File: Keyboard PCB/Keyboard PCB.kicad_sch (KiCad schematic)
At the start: 9 parts, among them SW1 SW_Push, SW2 SW_Push, SW3 SW_Push, SW4 SW_Push, SW5 SW_Push, SW6 SW_Push, U1 MOUDLE-SEEEDUINO-XIAO

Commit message: Who needs autosaves?
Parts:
- removed D1, D2: SK6812MINI-E, footprints:SK6812MINI-E_fixed, symbol SK6812MINI-E:SK6812MINI-E
- added D1, D2: SK6812MINI, LED_SMD:LED_SK6812MINI_PLCC4_3.5x3.5mm_P1.75mm, symbol LED:SK6812MINI
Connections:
- net +5V: now also D1.4 (VDD), D2.4 (VDD)
- net GND: now also D1.2 (VSS), D2.2 (VSS)
- net at U1.5 (PA8_A4_D4_SDA): now also D1.3 (DIN)
- new net: D1.1 (DOUT), D2.3 (DIN)

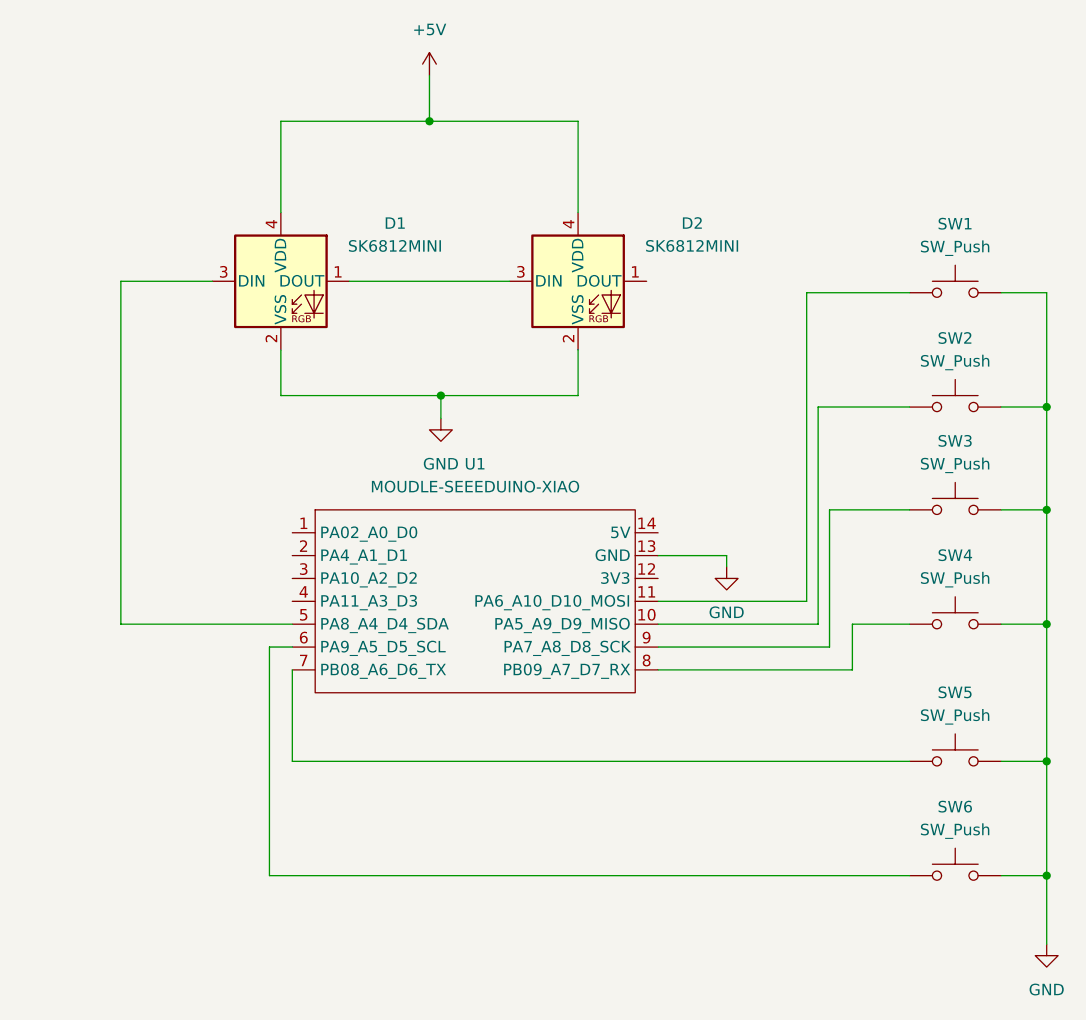
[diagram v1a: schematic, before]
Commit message: Adjusted wiring
I flipped the XIAO microcontroller because I was worried it would mess up the build process if it was on the bottom. For some reason the tutorial says to put it on the back side but most people just put it on top.
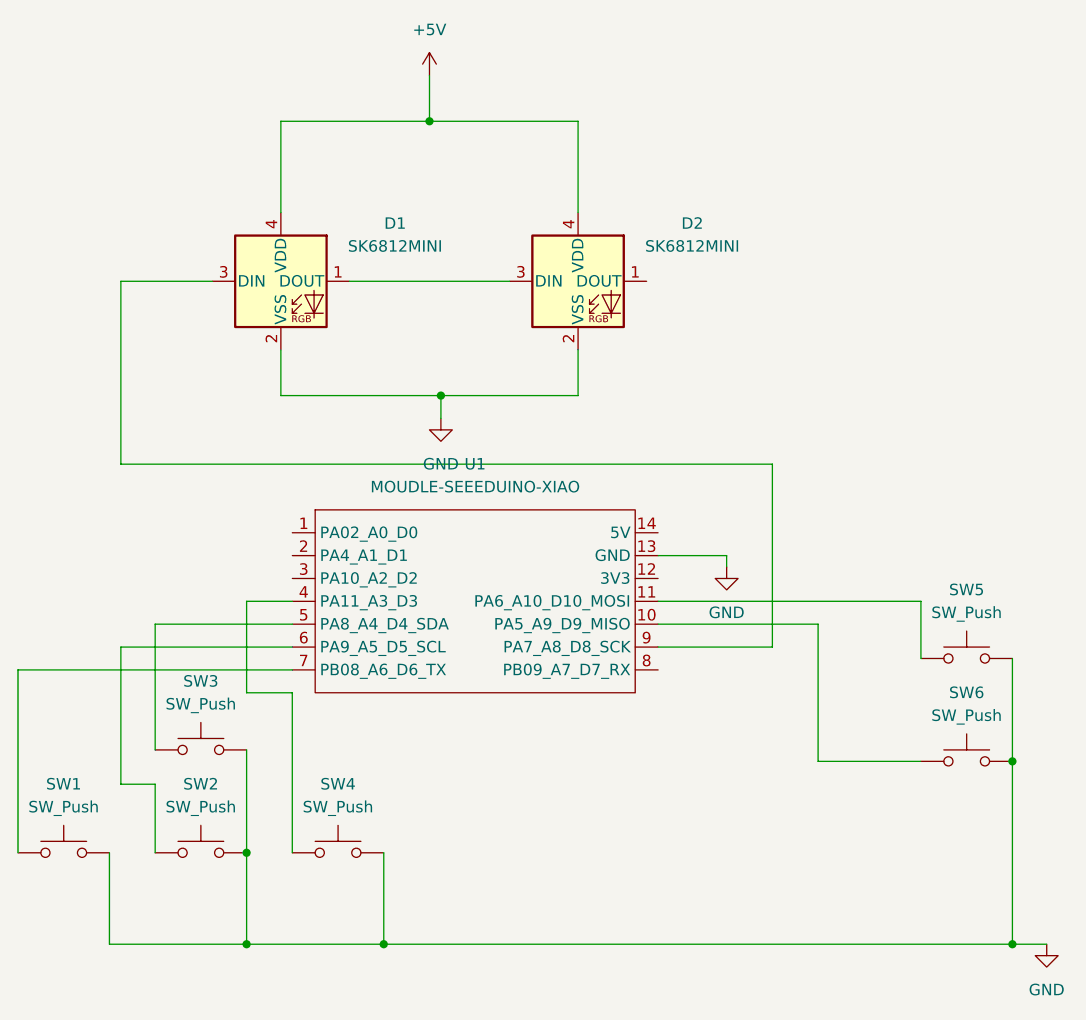
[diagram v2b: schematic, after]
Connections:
- net at SW5.1: now also U1.11 (PA6_A10_D10_MOSI); no longer U1.7 (PB08_A6_D6_TX)
- net at SW4.1: now also U1.4 (PA11_A3_D3); no longer U1.8 (PB09_A7_D7_RX)
- net at SW2.1: now also U1.6 (PA9_A5_D5_SCL); no longer U1.10 (PA5_A9_D9_MISO)
- net at SW3.1: now also U1.5 (PA8_A4_D4_SDA); no longer U1.9 (PA7_A8_D8_SCK)
- net at SW6.1: now also U1.10 (PA5_A9_D9_MISO); no longer U1.6 (PA9_A5_D5_SCL)
- net at D1.3 (DIN): now also U1.9 (PA7_A8_D8_SCK); no longer U1.5 (PA8_A4_D4_SDA)
- net at SW1.1: now also U1.7 (PB08_A6_D6_TX); no longer U1.11 (PA6_A10_D10_MOSI)
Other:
- moved on the sheet: SW1, SW2, SW3, SW4, SW5, SW6
